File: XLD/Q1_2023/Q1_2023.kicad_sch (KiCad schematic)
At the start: 9 parts

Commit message: done
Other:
- sheet QW5Q_gold QBlox1 ports: added 20_mod16_i1, 20_mod18_i1, 20_ro_out_mod12_mod16, 20_ro_out_mod12_mod18; removed 20_mod10_o1, 20_mod10_o2, 20_mod12_o1, 20_mod12_o2, 20_mod14_o1, 20_mod14_o2, 20_mod14_o3, 20_mod14_o4, 20_mod19_o1, 20_mod19_o2, 20_mod19_o3, 20_mod19_o4, 20_mod6_o1, 20_mod6_o2, 20_ro_in_mod16_mod18, 20_ro_out_mod16_mod18

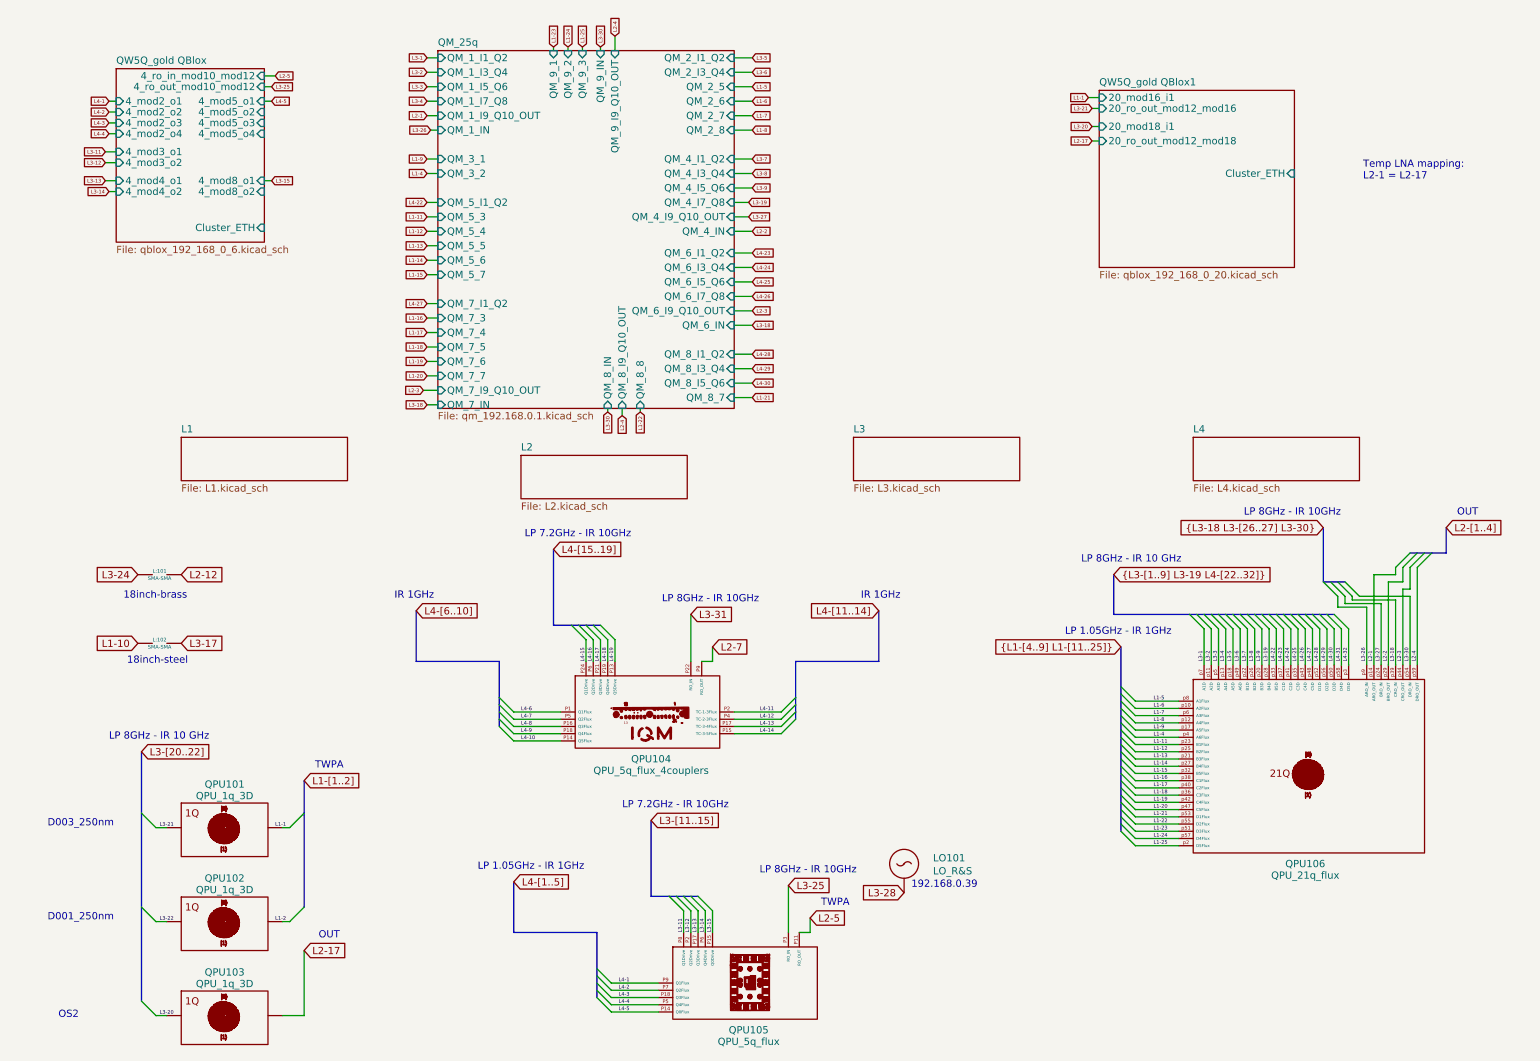
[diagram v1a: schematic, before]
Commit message: Corrected but path not verified
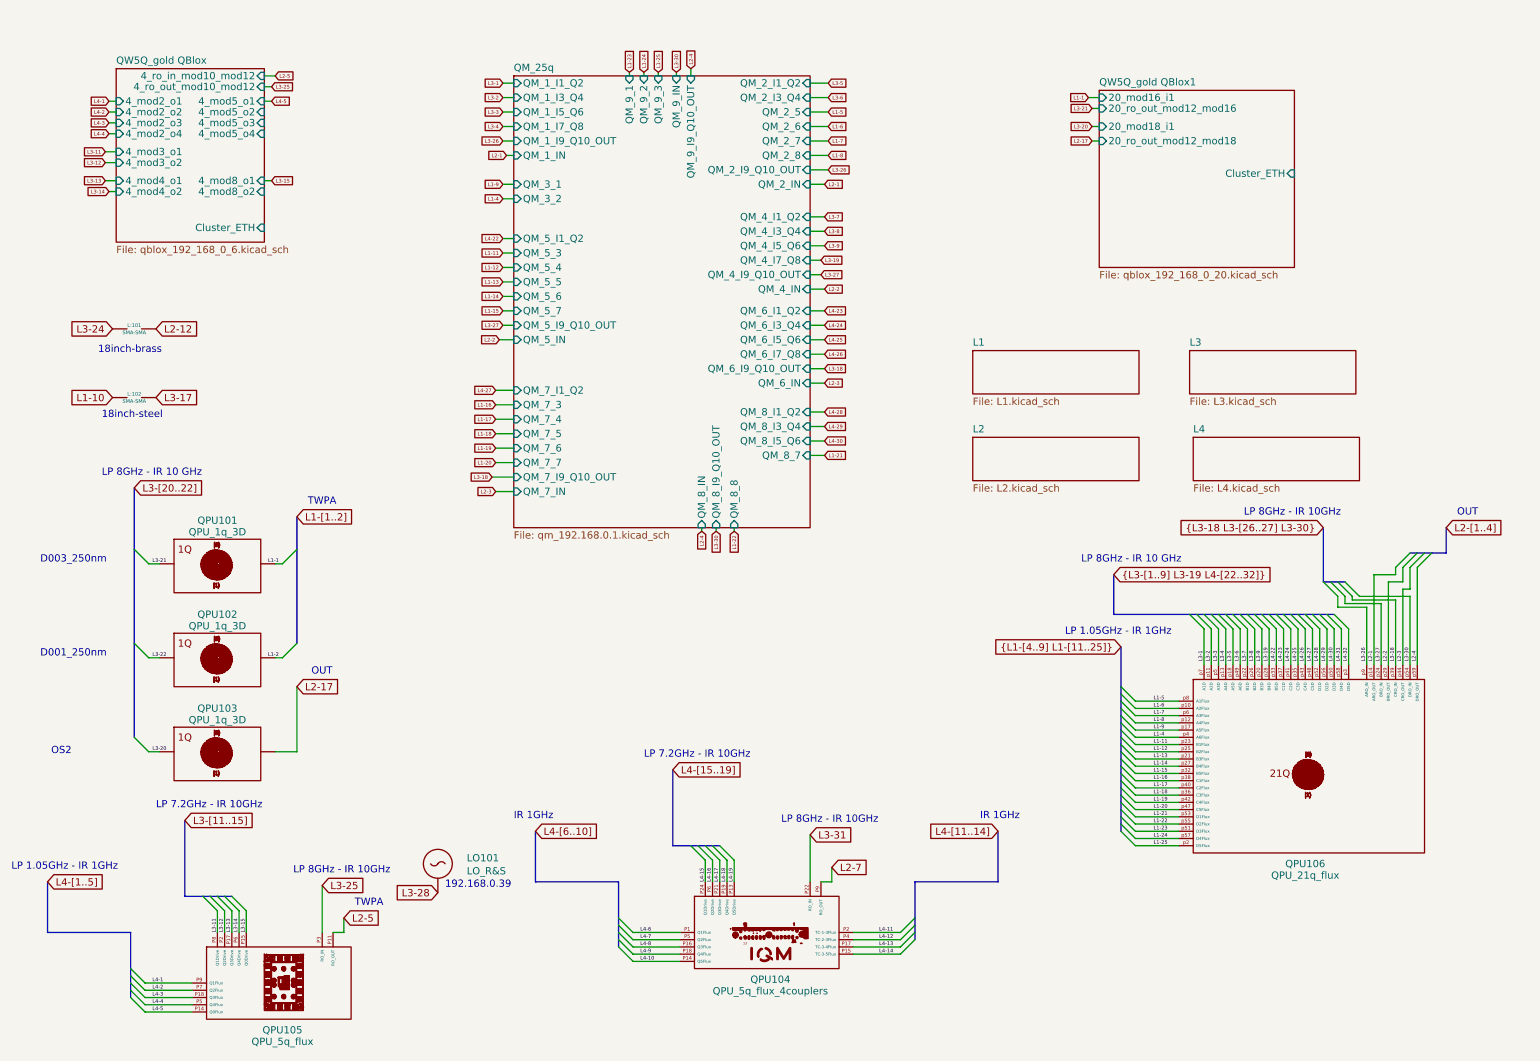
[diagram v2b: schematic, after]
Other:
- sheet QM_25q ports: added QM_2_I9_Q10_OUT, QM_2_IN, QM_5_I9_Q10_OUT, QM_5_IN; removed none
- note removed: "Temp LNA mapping: L2-1 = L2-17"
- moved on the sheet: L:101, L:102, LO101, QPU101, QPU102, QPU103, QPU104, QPU105

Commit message: filter fixed'
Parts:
- renumbered L:101 to L:?, L:102 to L:?, LO101 to LO?, QPU104 to QPU?, QPU101 to QPU?, QPU103 to QPU?, QPU102 to QPU?, QPU105 to QPU?, QPU106 to QPU?
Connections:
- net L3-28: no longer LO?.
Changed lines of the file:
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@@
   (symbol (lib_id "Quantum Computing:SMA-SMA") (at 34.925 66.04 0) (unit 1)
     (in_bom yes) (on_board yes) (dnp no) (fields_autoplaced)
-    (property "Reference" "L:101" (at 34.925 65.405 0)
+    (property "Reference" "L:?" (at 34.925 65.405 0)
       (effects (font (size 0.64 0.64)))
     )
@@
       (project "Q1_2023"
         (path "/9924af8b-9fcb-4325-a1dc-18dd2c4184d7"
-          (reference "L:101") (unit 1)
+          (reference "L:?") (unit 1)
         )
       )
@@
   (symbol (lib_id "Quantum Computing:QPU_5q_flux_4couplers") (at 152.4 178.435 0) (unit 1)
     (in_bom yes) (on_board no) (dnp no) (fields_autoplaced)
-    (property "Reference" "QPU104" (at 146.685 180.34 0)
+    (property "Reference" "QPU?" (at 146.685 180.34 0)
       (effects (font (size 1.27 1.27)))
     )
@@
       (project "Q1_2023"
         (path "/9924af8b-9fcb-4325-a1dc-18dd2c4184d7"
-          (reference "QPU104") (unit 1)
+          (reference "QPU?") (unit 1)
         )
       )
@@
   (symbol (lib_id "Quantum Computing:QPU_1q_3D") (at 49.53 107.315 0) (unit 1)
     (in_bom yes) (on_board no) (dnp no) (fields_autoplaced)
-    (property "Reference" "QPU101" (at 49.53 99.695 0)
+    (property "Reference" "QPU?" (at 49.53 99.695 0)
       (effects (font (size 1.27 1.27)))
     )
@@
       (project "Q1_2023"
         (path "/9924af8b-9fcb-4325-a1dc-18dd2c4184d7"
-          (reference "QPU101") (unit 1)
+          (reference "QPU?") (unit 1)
         )
       )
@@
   (symbol (lib_id "Quantum Computing:QPU_1q_3D") (at 49.53 140.335 0) (unit 1)
     (in_bom yes) (on_board no) (dnp no) (fields_autoplaced)
-    (property "Reference" "QPU103" (at 49.53 132.715 0)
+    (property "Reference" "QPU?" (at 49.53 132.715 0)
       (effects (font (size 1.27 1.27)))
     )
@@
       (project "Q1_2023"
         (path "/9924af8b-9fcb-4325-a1dc-18dd2c4184d7"
-          (reference "QPU103") (unit 1)
+          (reference "QPU?") (unit 1)
         )
       )
@@
   (symbol (lib_id "Quantum Computing:LO_R&S") (at 88.265 160.02 0) (unit 1)
     (in_bom yes) (on_board no) (dnp no) (fields_autoplaced)
-    (property "Reference" "LO101" (at 93.345 159.004 0)
+    (property "Reference" "LO?" (at 95.885 159.004 0)
       (effects (font (size 1.27 1.27)) (justify left))
     )
-    (property "Value" "LO_R&S" (at 93.345 161.29 0)
+    (property "Value" "LO_R&S" (at 95.885 161.29 0)
       (effects (font (size 1.27 1.27)) (justify left))
     )
@@
       (project "Q1_2023"
         (path "/9924af8b-9fcb-4325-a1dc-18dd2c4184d7"
-          (reference "LO101") (unit 1)
+          (reference "LO?") (unit 1)
         )
       )
@@
   (symbol (lib_id "Quantum Computing:SMA-SMA") (at 34.925 78.105 0) (unit 1)
     (in_bom yes) (on_board yes) (dnp no) (fields_autoplaced)
-    (property "Reference" "L:102" (at 34.925 77.47 0)
+    (property "Reference" "L:?" (at 34.925 77.47 0)
       (effects (font (size 0.64 0.64)))
     )
@@
       (project "Q1_2023"
         (path "/9924af8b-9fcb-4325-a1dc-18dd2c4184d7"
-          (reference "L:102") (unit 1)
+          (reference "L:?") (unit 1)
         )
       )
@@
   (symbol (lib_id "Quantum Computing:QPU_1q_3D") (at 49.53 123.825 0) (unit 1)
     (in_bom yes) (on_board no) (dnp no) (fields_autoplaced)
-    (property "Reference" "QPU102" (at 49.53 116.205 0)
+    (property "Reference" "QPU?" (at 49.53 116.205 0)
       (effects (font (size 1.27 1.27)))
     )
@@
       (project "Q1_2023"
         (path "/9924af8b-9fcb-4325-a1dc-18dd2c4184d7"
-          (reference "QPU102") (unit 1)
+          (reference "QPU?") (unit 1)
         )
       )
@@
   (symbol (lib_id "Quantum Computing:QPU_5q_flux") (at 66.675 187.325 0) (unit 1)
     (in_bom yes) (on_board no) (dnp no) (fields_autoplaced)
-    (property "Reference" "QPU105" (at 60.96 189.23 0)
+    (property "Reference" "QPU?" (at 60.96 189.23 0)
       (effects (font (size 1.27 1.27)))
     )
@@
       (project "Q1_2023"
         (path "/9924af8b-9fcb-4325-a1dc-18dd2c4184d7"
-          (reference "QPU105") (unit 1)
+          (reference "QPU?") (unit 1)
         )
       )
@@
   (symbol (lib_id "Quantum Computing:QPU_21q_flux") (at 241.3 158.115 0) (unit 1)
     (in_bom yes) (on_board no) (dnp no) (fields_autoplaced)
-    (property "Reference" "QPU106" (at 240.665 160.02 0)
+    (property "Reference" "QPU?" (at 240.665 160.02 0)
       (effects (font (size 1.27 1.27)))
     )
@@
       (project "Q1_2023"
         (path "/9924af8b-9fcb-4325-a1dc-18dd2c4184d7"
-          (reference "QPU106") (unit 1)
-        )
-      )
+          (reference "QPU?") (unit 1)
+        )
+      )
